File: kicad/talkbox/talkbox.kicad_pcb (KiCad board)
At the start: 2 copper layers, 89 x 59.9 mm, 44 parts, among them J1 AudioJack2, J2 Conn_01x02, J3 AudioJack2, J4 Barrel_Jack_Switch, SW1 SW_SPST, U1 LM386, U2 SW_3PDT, U3 TL071, U4 LT1054xSOIC16, U5 LM7812_TO220, U6 LM7912_TO220

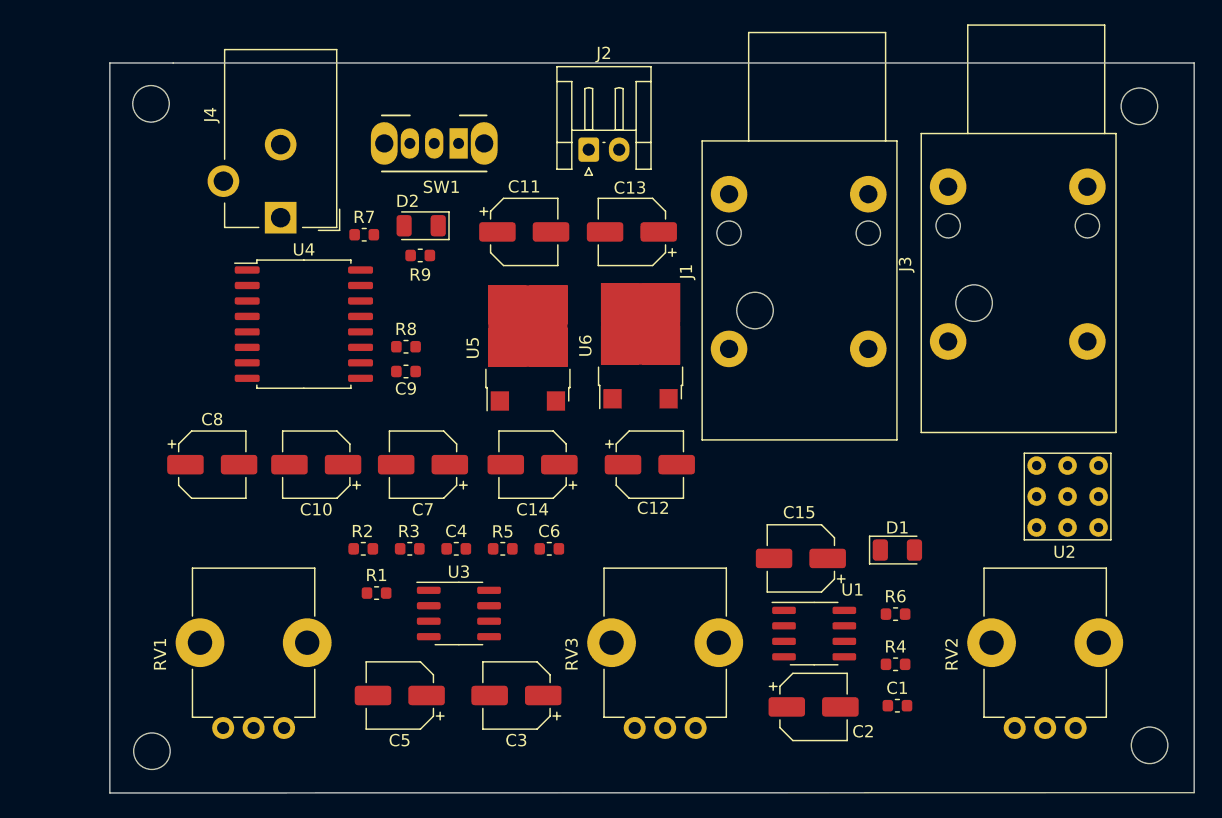
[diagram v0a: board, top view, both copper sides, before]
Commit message: Added kicad libraries and updated pcb
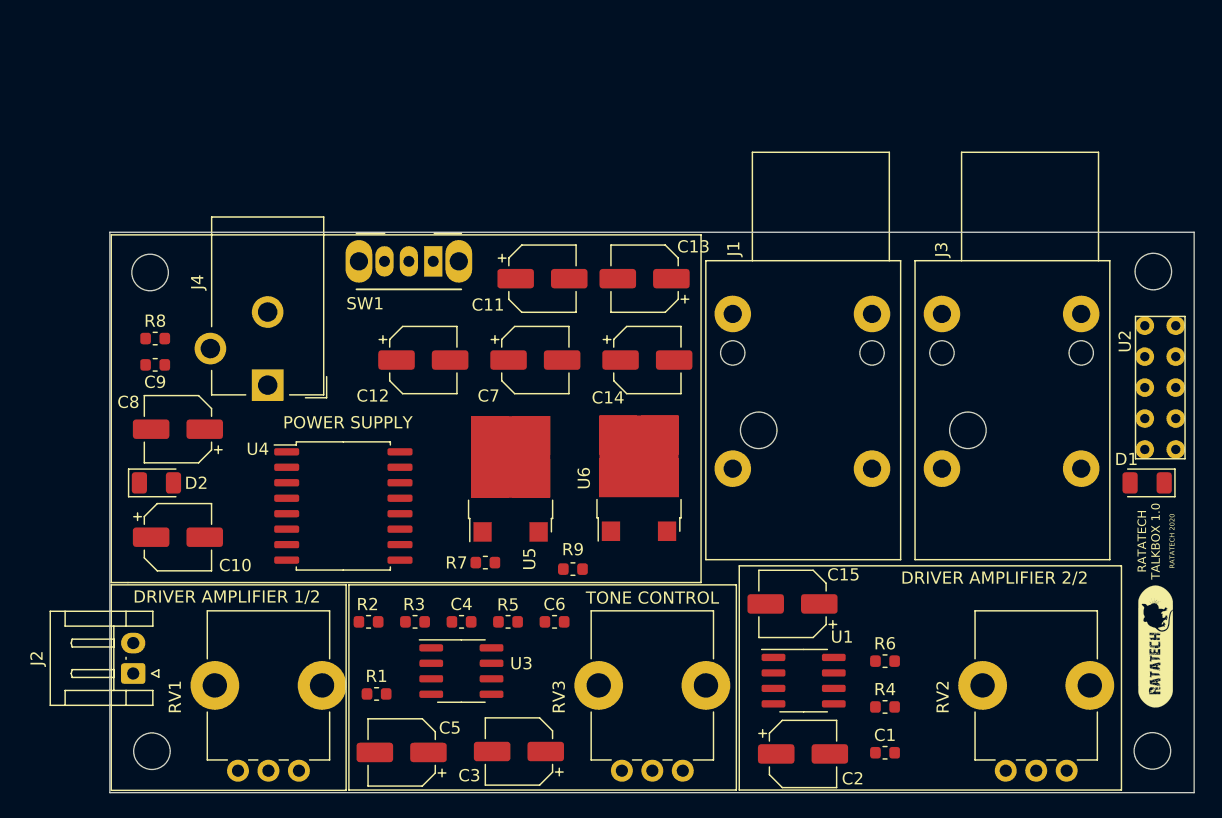
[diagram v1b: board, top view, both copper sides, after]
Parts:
- added G***: LOGO, imgs:ratatech_bitmap_10x2.8mm, F.Cu at (169.4, 108.0)
- moved J2 57.0 mm to (85.5, 110.2), turned to 90 degrees
- moved D2 30.3 mm to (87.4, 94.6), turned to 0 degrees
- moved R7 28.7 mm to (114.4, 101.1)
- moved R9 28.6 mm to (121.6, 101.6), turned to 180 degrees
- moved D1 21.2 mm to (168.7, 94.6), turned to 180 degrees
- moved R8 20.6 mm to (87.3, 82.7)
- moved C9 20.6 mm to (87.3, 84.9)
- moved C12 20.5 mm to (109.3, 84.5)
- moved U4 15.3 mm to (102.8, 96.5)
- moved REF0 13.8 mm to (86.9, 77.3)
- moved REF1 13.6 mm to (169.2, 77.2), turned to 90 degrees
- moved C10 12.8 mm to (89.2, 99.0), turned to 0 degrees
- moved C14 12.7 mm to (127.7, 84.5), turned to 0 degrees
- moved C7 12.6 mm to (118.5, 84.5), turned to 0 degrees
- moved U2 11.5 mm to (169.8, 87.0), turned to 90 degrees
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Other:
- board size 89 x 59.9 mm -> 89 x 46 mm
- board text added: "DRIVER AMPLIFIER 1/2"
- board text added: "DRIVER AMPLIFIER 2/2"
- board text added: "POWER SUPPLY"
- board text added: "RATATECH 2020"
- board text added: "RATATECH TALKBOX 1.0"
- board text added: "TONE CONTROL"

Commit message: Added gitignore
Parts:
- moved U1 1.52 mm to (142.0, 110.4)
- moved C1 1.52 mm to (148.7, 116.4)
- moved C2 1.52 mm to (142.0, 116.5)
- moved R4 1.52 mm to (148.7, 112.6)
- moved R6 1.52 mm to (148.7, 108.8)
- moved C4 0.74 mm to (112.7, 105.3)
- moved C6 0.74 mm to (120.3, 105.3)
- moved R2 0.74 mm to (105.1, 105.3)
- moved R3 0.74 mm to (108.9, 105.3)
- moved R5 0.74 mm to (116.5, 105.3)
- moved REF0 0.28 mm to (87.0, 77.5)
- moved G*** 0.21 mm to (169.6, 108.1)
- moved REF1 0.10 mm to (169.2, 77.3), turned to 0 degrees
- moved REF3 0.10 mm to (87.0, 116.6)
- moved REF2 0.09 mm to (169.2, 116.6)
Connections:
- R1 pad 1: Net-(R1-Pad1) -> tone_control_output
- RV3 pad 3: Net-(R1-Pad1) -> tone_control_output

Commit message: First time routing
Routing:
- net GND: track 0.00 -> 311.7 mm
- net VCC: track 0.00 -> 118.7 mm
- net Net-(J2-Pad1): track 0.00 -> 110.0 mm
- net Net-(C10-Pad2): track 0.00 -> 97.8 mm
- net input: track 0.00 -> 92.7 mm, vias 0 -> 1
- net Net-(C11-Pad1): track 0.00 -> 59.5 mm
- net tone_control_output: track 0.00 -> 49.5 mm
- net Net-(RV1-Pad2): track 0.00 -> 47.1 mm
- net VDD: track 0.00 -> 45.9 mm, vias 0 -> 2
- net Net-(D2-Pad2): track 0.00 -> 40.8 mm
- net Net-(R6-Pad2): track 0.00 -> 38.1 mm
- net Net-(C9-Pad2): track 0.00 -> 36.8 mm
- net output: track 0.00 -> 30.1 mm
- net Net-(D1-Pad2): track 0.00 -> 25.3 mm
- net Net-(C2-Pad1): track 0.00 -> 24.1 mm
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- added copper zone on B.Cu, net GND
- added copper zone on F.Cu, net GND

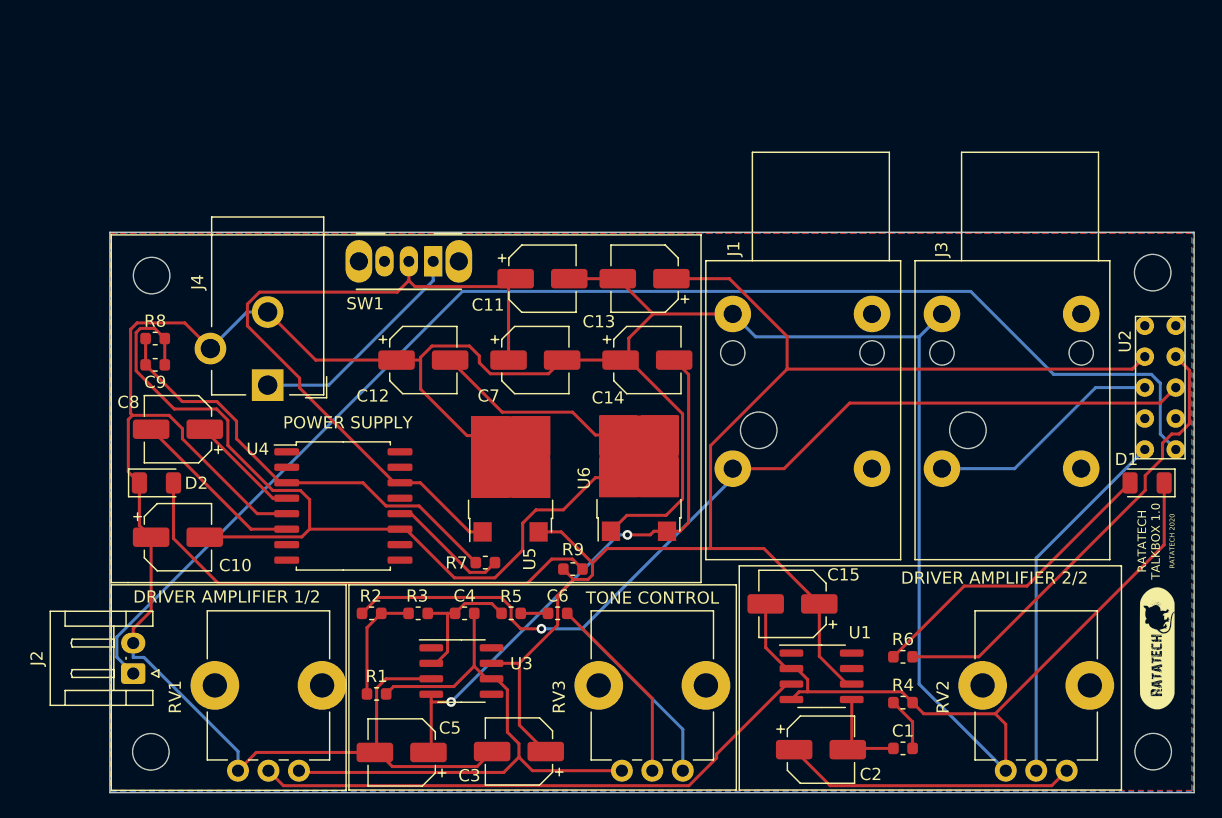
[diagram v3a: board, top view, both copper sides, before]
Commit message: Added tl072 and preamp stage
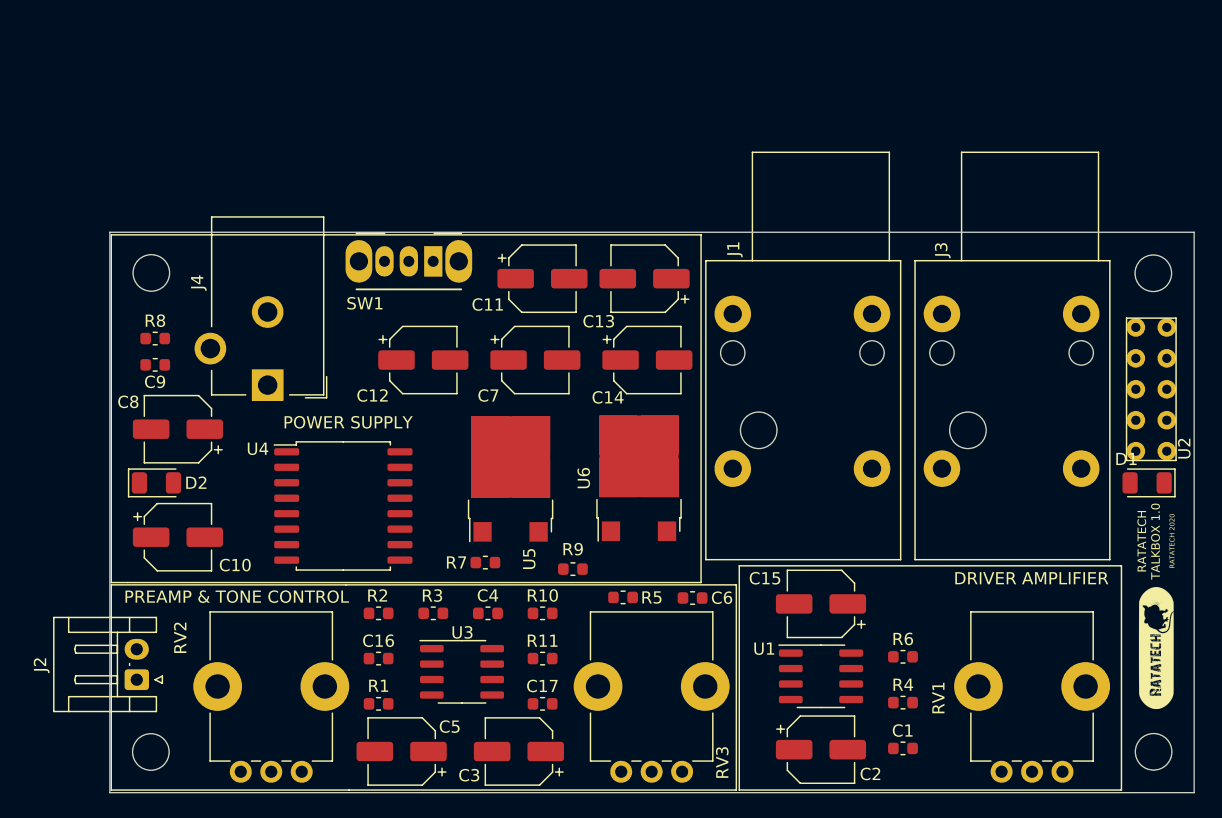
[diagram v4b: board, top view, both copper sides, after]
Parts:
- removed G***: LOGO, imgs:ratatech_bitmap_10x2.8mm
- removed REF0, REF1, REF2, REF3: MountingHole_3mm, MountingHole:MountingHole_3mm
- added C16: 10uF, Capacitor_SMD:C_0603_1608Metric, F.Cu at (105.7, 109.0)
- added C17: 10uF, Capacitor_SMD:C_0603_1608Metric, F.Cu at (119.1, 112.7)
- added H1: MountingHole, MountingHole:MountingHole_3mm, F.Cu at (87.0, 77.3)
- added H2: MountingHole, MountingHole:MountingHole_3mm, F.Cu at (169.2, 77.4)
- added H3: MountingHole, MountingHole:MountingHole_3mm, F.Cu at (87.0, 116.6)
- added H4: MountingHole, MountingHole:MountingHole_3mm, F.Cu at (169.3, 116.6)
- added R10: 1000k, Resistor_SMD:R_0603_1608Metric, F.Cu at (119.1, 105.3)
- added R11: 10K, Resistor_SMD:R_0603_1608Metric, F.Cu at (119.1, 109.0)
- added U7: logo, imgs:ratatech_bitmap_10x2.8mm, F.Cu at (169.5, 108.1)
- RV2: value 10K -> 20K
- U3: value TL071 -> TL072
- moved RV2 62.8 mm to (96.8, 110.9)
- moved RV1 62.7 mm to (159.2, 110.9)
- moved C6 11.1 mm to (131.4, 104.0)
- moved R5 9.28 mm to (125.7, 104.0)
- moved C15 2.34 mm to (142.0, 104.5)
- moved C4 1.91 mm to (114.6, 105.3)
- moved R3 1.24 mm to (110.1, 105.3)
- moved R1 0.83 mm to (105.7, 112.7)
- moved U2 0.75 mm to (169.1, 87.1)
- moved J2 0.59 mm to (85.8, 110.7)
- moved R2 0.57 mm to (105.7, 105.3)
- moved RV3 0.11 mm to (128.0, 110.9)
- moved U3 0.08 mm to (112.5, 110.1)
- moved C5 0.08 mm to (107.5, 116.6)
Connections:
- C2 pad 1: Net-(C2-Pad1) -> output
- C5 pad 1: VDD -> GND
- C5 pad 2: GND -> VDD
- RV1 pad 1: tone_control_output -> preamp_output
- RV2 pad 1: Net-(C2-Pad1) -> Net-(R11-Pad2)
- RV2 pad 2: output -> Net-(R11-Pad2)
- RV2 pad 3: GND -> preamp_output
- U3 pad 1: (no net) -> tone_control_output
- U3 pad 5: (no net) -> Net-(C17-Pad2)
- U3 pad 6: tone_control_output -> Net-(R11-Pad2)
- U3 pad 7: VCC -> preamp_output
- U3 pad 8: (no net) -> VCC
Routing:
- net GND: track 311.7 -> 0.00 mm
- net VCC: track 118.7 -> 0.00 mm
- net Net-(J2-Pad1): track 110.0 -> 0.00 mm
- net Net-(C10-Pad2): track 97.8 -> 0.00 mm
- net input: track 92.7 -> 0.00 mm, vias 1 -> 0
- net Net-(C11-Pad1): track 59.5 -> 0.00 mm
- net tone_control_output: track 49.5 -> 0.00 mm
- net Net-(RV1-Pad2): track 47.1 -> 0.00 mm
- net VDD: track 45.9 -> 0.00 mm, vias 2 -> 0
- net Net-(D2-Pad2): track 40.8 -> 0.00 mm
- net Net-(R6-Pad2): track 38.1 -> 0.00 mm
- net Net-(C9-Pad2): track 36.8 -> 0.00 mm
- net output: track 30.1 -> 0.00 mm
- net Net-(D1-Pad2): track 25.3 -> 0.00 mm
- net Net-(C2-Pad1): track 24.1 -> 0.00 mm
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- removed copper zone on B.Cu, net GND
- removed copper zone on F.Cu, net GND
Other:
- board text added: "DRIVER AMPLIFIER"
- board text added: "PREAMP & TONE CONTROL"
- board text removed: "DRIVER AMPLIFIER 1/2"
- board text removed: "DRIVER AMPLIFIER 2/2"
- board text removed: "TONE CONTROL"

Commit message: Removed lm386 based power amplifier and adapted tone control
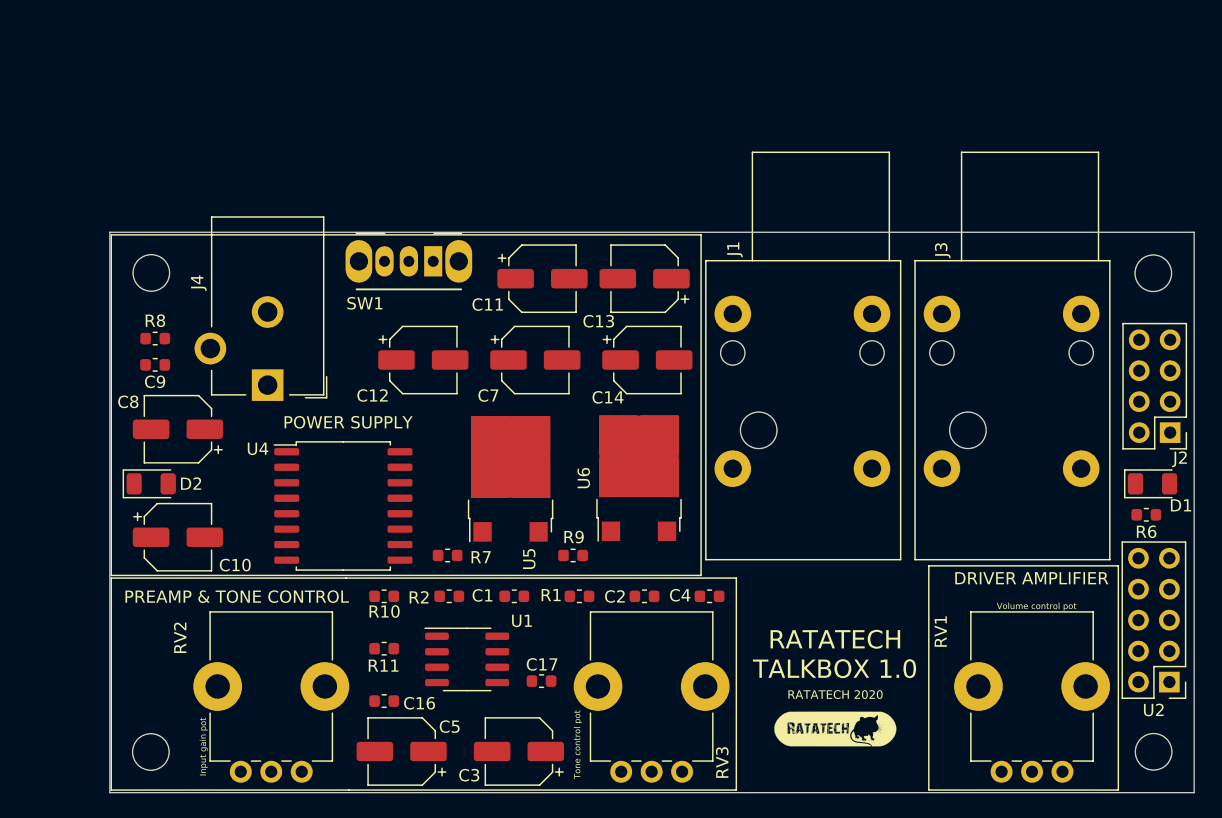
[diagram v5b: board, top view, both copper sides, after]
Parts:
- removed C15: 100uF, Capacitor_SMD:CP_Elec_5x5.3
- removed C6: 4.7nF, Capacitor_SMD:C_0603_1608Metric
- removed R3: 22K, Resistor_SMD:R_0603_1608Metric
- removed R4: 10, Resistor_SMD:R_0603_1608Metric
- removed R5: 9.1K, Resistor_SMD:R_0603_1608Metric
- removed U3: TL072, Package_SO:SOIC-8_3.9x4.9mm_P1.27mm
- C1: value 0.05uF -> 4.7nF
- C2: value 20uF -> 4.7nF; footprint Capacitor_SMD:CP_Elec_5x5.3 -> Capacitor_SMD:C_0603_1608Metric
- J2: value Conn_01x02 -> Conn_02x04_Odd_Even; footprint Connector_JST:JST_EH_S2B-EH_1x02_P2.50mm_Horizontal -> Connector_PinHeader_2.54mm:PinHeader_2x04_P2.54mm_Vertical
- R1, R2: value 1.8K -> 9.1K
- R11: value 10K -> 2k
- U1: value LM386 -> TL071
- U2: footprint Stompbox_Switch:SW_Stompbox_3PDT_redux -> Connector_PinHeader_2.54mm:PinHeader_2x05_P2.54mm_Vertical
- moved J2 87.2 mm to (170.6, 90.4), turned to 180 degrees
- moved C1 34.3 mm to (116.8, 103.9), turned to 180 degrees
- moved U1 29.1 mm to (112.9, 109.1)
- moved U7 27.2 mm to (143.1, 114.8), turned to 0 degrees
- moved U2 23.8 mm to (170.6, 110.9), turned to 180 degrees
- moved R6 23.1 mm to (168.7, 97.2), turned to 180 degrees
- moved C2 19.2 mm to (127.5, 103.9)
- moved R1 18.7 mm to (122.1, 103.9)
- moved C4 18.2 mm to (132.8, 103.9)
- moved R10 13.1 mm to (106.1, 103.9)
- moved R11 13.0 mm to (106.1, 108.2)
- moved R2 5.96 mm to (111.5, 103.9)
- moved C16 3.52 mm to (106.1, 112.5)
- moved R7 3.15 mm to (111.3, 100.5)
- moved C17 1.87 mm to (119.0, 110.8), turned to 180 degrees
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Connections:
- C1 pad 2: Net-(C1-Pad2) -> driver_-
- C10 pad 1: GND -> driver_-
- C11 pad 2: GND -> driver_-
- C12 pad 1: GND -> driver_-
- C13 pad 2: GND -> driver_-
- C14 pad 1: GND -> driver_-
- C16 pad 2: GND -> driver_-
- C17 pad 1: tone_control_output -> input
- C2 pad 1: output -> (no net)
- C2 pad 2: Net-(C1-Pad1) -> Net-(C2-Pad2)
- C3 pad 2: GND -> driver_-
- C4 pad 1: Net-(C4-Pad1) -> preamp_output
- C4 pad 2: tone_control_output -> Net-(C4-Pad2)
- C5 pad 1: GND -> driver_-
- C7 pad 2: GND -> driver_-
- D1 pad 1: GND -> driver_-
- D2 pad 1: GND -> driver_-
- J1 pad S: GND -> driver_-
- J2 pad 1: Net-(J2-Pad1) -> pa_input
- J2 pad 2: GND -> driver_-
- J3 pad S: GND -> driver_-
- J4 pad 2: GND -> driver_-
- J4 pad 3: GND -> driver_-
- R1 pad 1: tone_control_output -> Net-(C1-Pad1)
- R1 pad 2: Net-(R1-Pad2) -> preamp_output
- R10 pad 1: GND -> driver_-
- R2 pad 1: Net-(R1-Pad2) -> Net-(C4-Pad2)
- R2 pad 2: input -> driver_-
- RV1 pad 2: Net-(RV1-Pad2) -> pa_input
- RV1 pad 3: GND -> driver_-
- RV3 pad 1: input -> Net-(C4-Pad2)
- RV3 pad 2: Net-(C6-Pad2) -> Net-(C2-Pad2)
- RV3 pad 3: tone_control_output -> Net-(C1-Pad1)
- U1 pad 2: GND -> Net-(C17-Pad2)
- U1 pad 3: Net-(RV1-Pad2) -> Net-(R11-Pad2)
- U1 pad 4: GND -> VDD
- U1 pad 5: Net-(C1-Pad1) -> (no net)
- U1 pad 6: VCC -> preamp_output
- U1 pad 7: (no net) -> VCC
- U2 pad 1: output -> pa_output
- U2 pad 2: Net-(J2-Pad1) -> driver_+
- U4 pad 5: GND -> driver_-
- U5 pad 2: GND -> driver_-
- U6 pad 1: GND -> driver_-
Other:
- board text added: "Driver+"
- board text added: "Input gain pot"
- board text added: "Tone control pot"
- board text added: "Volume control pot"
- board text added: "driver+"
- board text added: "driver-"
- board text added: "input"
- board text added: "jack tip"
- board text added: "led"
- board text added: "pa_in"
- board text added: "pa_out"
- board text added: "vcc"
